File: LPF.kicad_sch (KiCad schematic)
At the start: 1 part

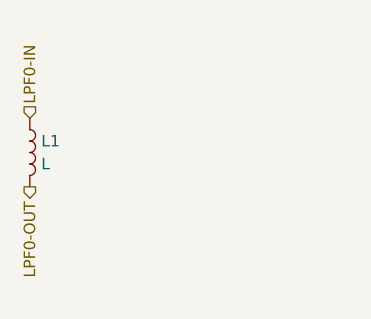
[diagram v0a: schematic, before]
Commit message: placed LPF chains in sub-schematic.  ERC passes
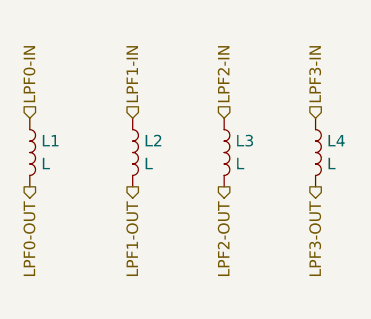
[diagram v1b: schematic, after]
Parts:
- added L2, L3, L4: L, symbol Device:L
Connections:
- new net LPF1-IN: L2.1
- new net LPF1-OUT: L2.2
- new net LPF2-IN: L3.1
- new net LPF2-OUT: L3.2
- new net LPF3-IN: L4.1
- new net LPF3-OUT: L4.2

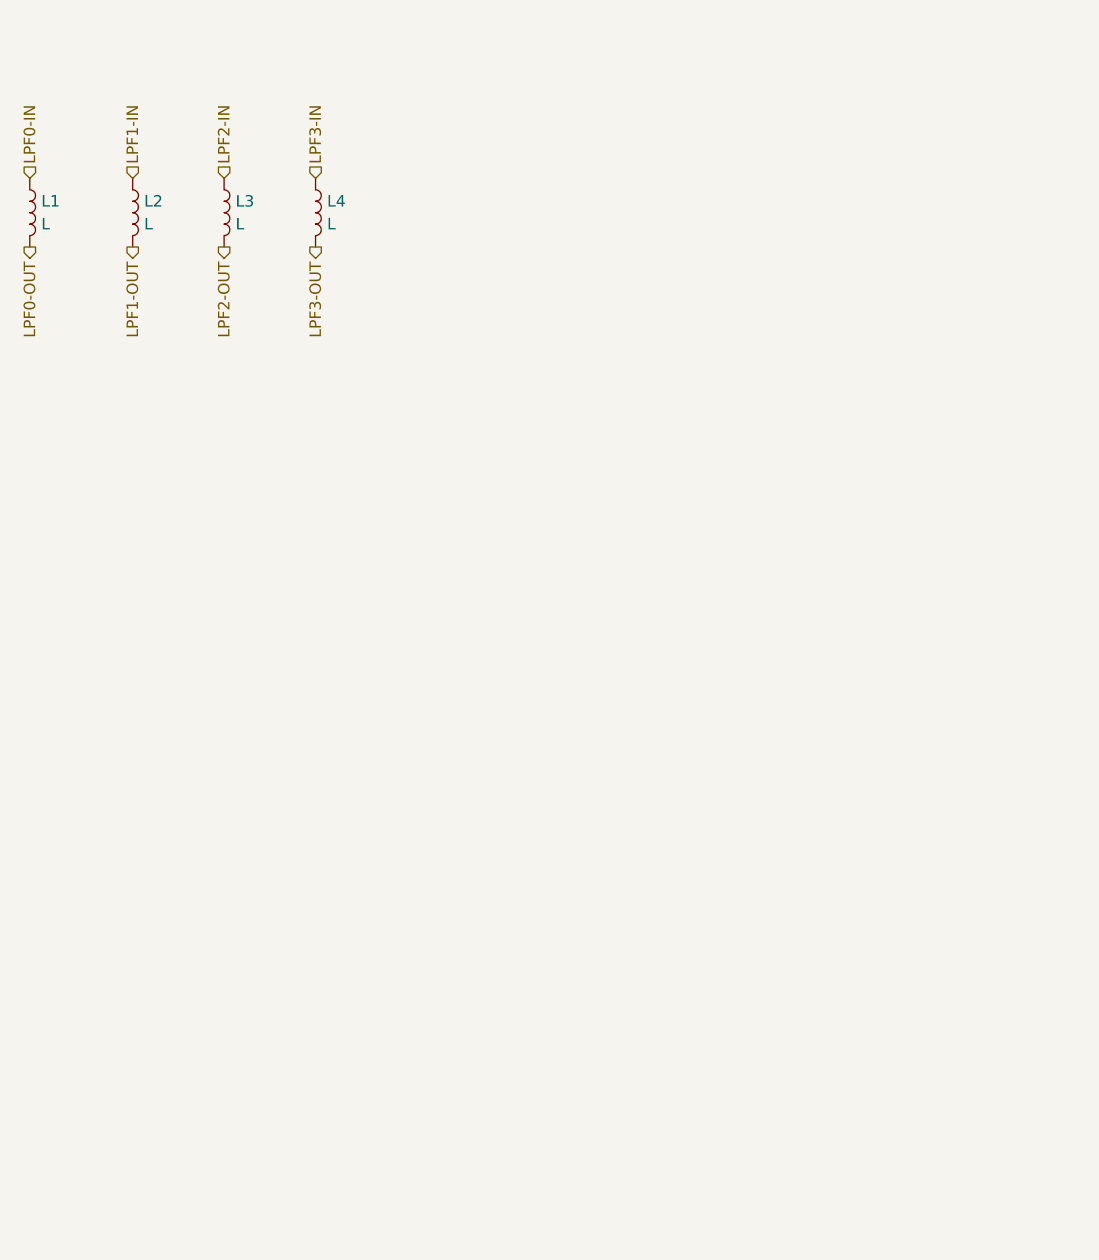
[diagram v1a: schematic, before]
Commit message: fleshed out LPF chains.  ERC passes
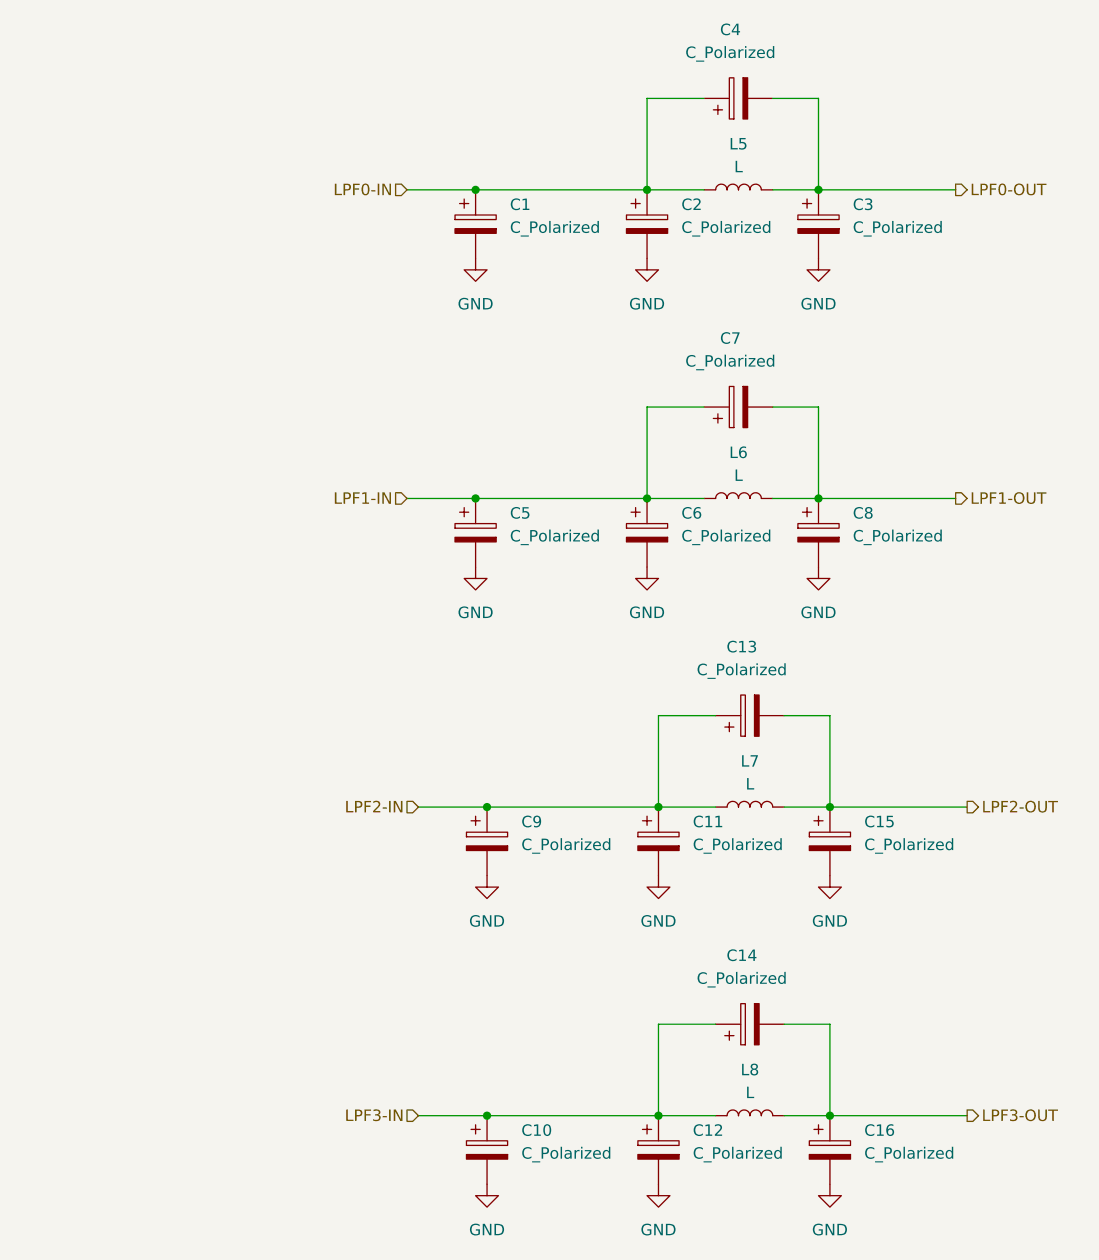
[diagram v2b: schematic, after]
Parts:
- removed L1, L2, L3, L4: L, symbol Device:L
- added C1, C10, C11, C12, C13, C14, C15, C16, C2, C3, C4, C5, C6, C7, C8, C9: C_Polarized, symbol Device:C_Polarized
- added L5, L6, L7, L8: L, symbol Device:L
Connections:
- net LPF0-IN: now also C1.1, C2.1, C4.1, L5.1
- net LPF0-OUT: now also C3.1, C4.2, L5.2
- net LPF1-IN: now also C5.1, C6.1, C7.1, L6.1
- net LPF1-OUT: now also C7.2, C8.1, L6.2
- net LPF2-IN: now also C11.1, C13.1, C9.1, L7.1
- net LPF2-OUT: now also C13.2, C15.1, L7.2
- net LPF3-IN: now also C10.1, C12.1, C14.1, L8.1
- net LPF3-OUT: now also C14.2, C16.1, L8.2
- new net GND: C1.2, C10.2, C11.2, C12.2, C15.2, C16.2, C2.2, C3.2, C5.2, C6.2, C8.2, C9.2

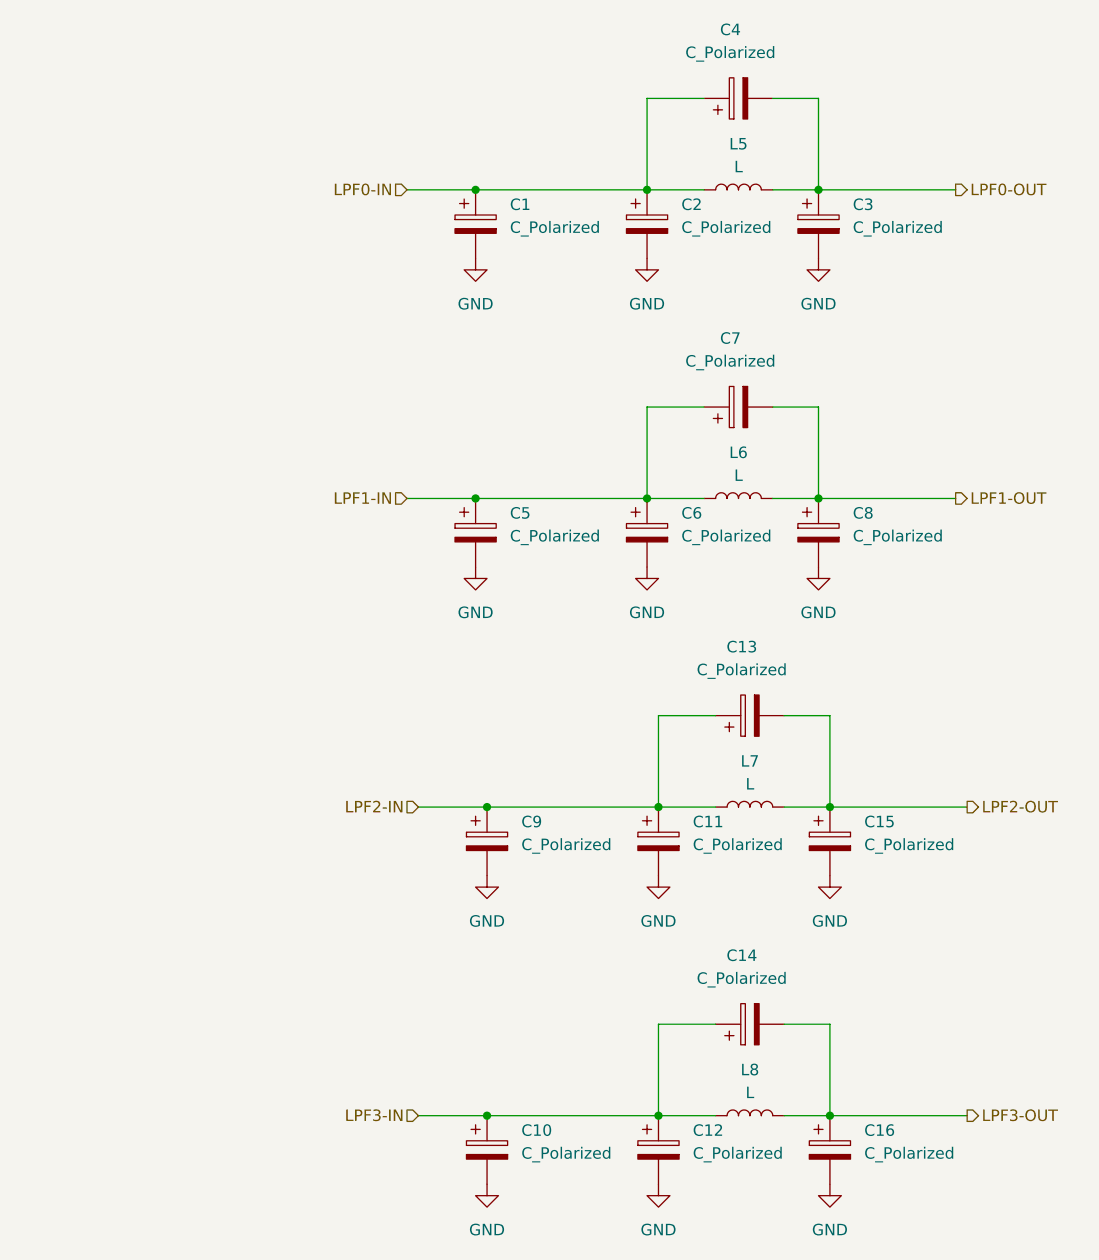
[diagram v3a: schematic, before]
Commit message: LPF chains, all caps now normal; missing inducator added.  ERC passes
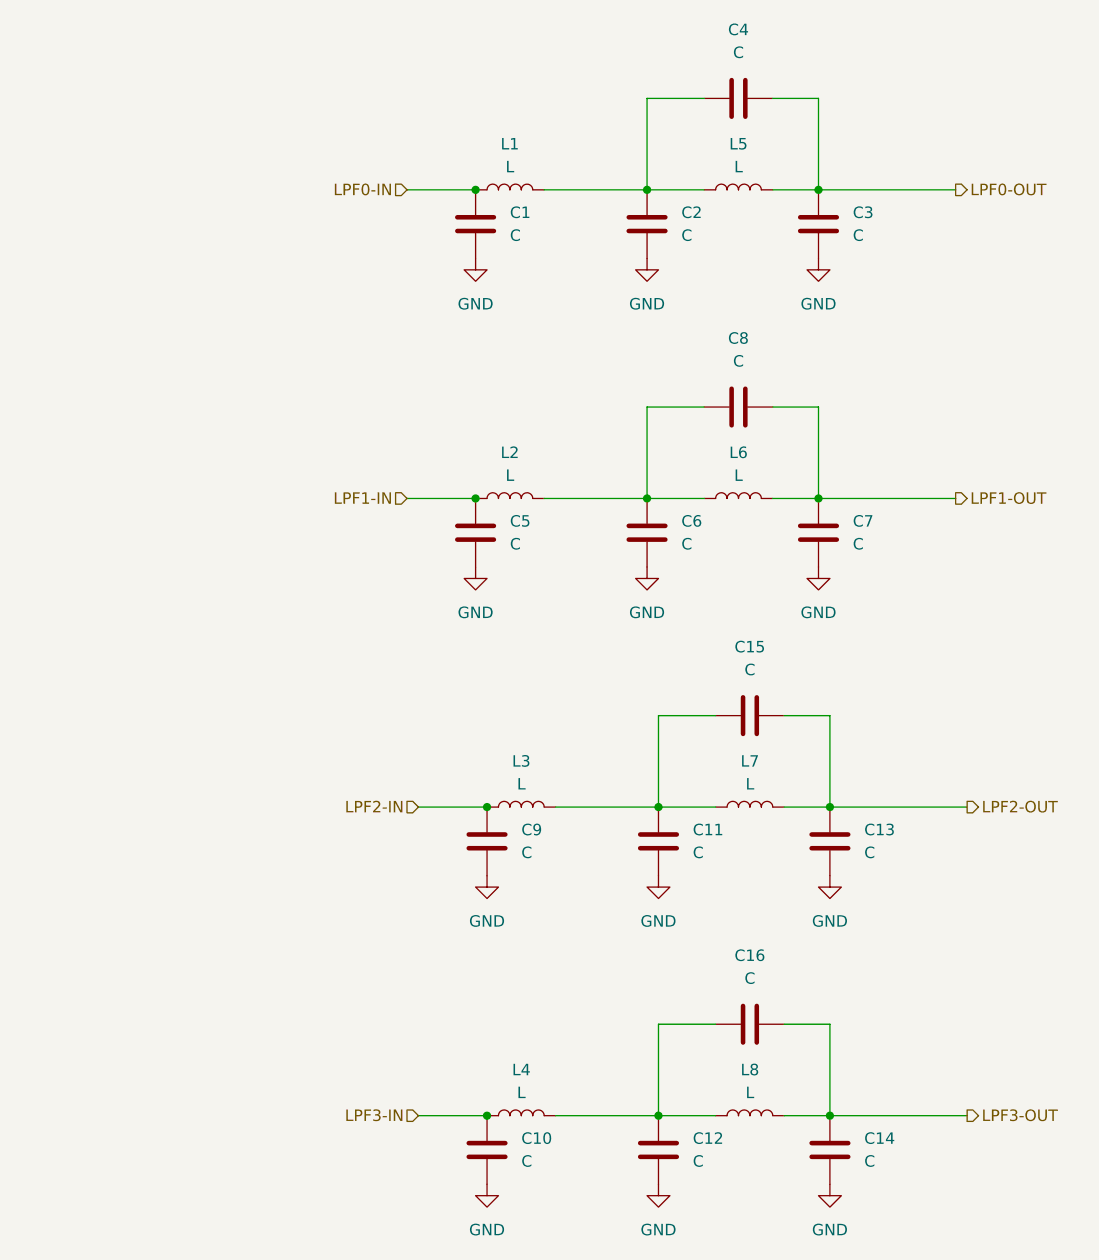
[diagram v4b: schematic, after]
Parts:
- removed C1, C10, C11, C12, C13, C14, C15, C16, C2, C3, C4, C5, C6, C7, C8, C9: C_Polarized, symbol Device:C_Polarized
- added C1, C10, C11, C12, C13, C14, C15, C16, C2, C3, C4, C5, C6, C7, C8, C9: C, symbol Device:C
- added L1, L2, L3, L4: L, symbol Device:L
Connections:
- net GND: now also C1.2, C10.2, C11.2, C12.2, C13.2, C14.2, C2.1, C3.2, C5.2, C6.2, C7.2, C9.2
- net LPF0-IN: now also C1.1, L1.1; no longer L5.1
- net LPF0-OUT: now also C3.1, C4.2
- net LPF1-IN: now also C5.1, L2.1; no longer L6.1
- net LPF1-OUT: now also C7.1, C8.2
- net LPF2-IN: now also C9.1, L3.1; no longer L7.1
- net LPF2-OUT: now also C13.1, C15.2
- net LPF3-IN: now also C10.1, L4.1; no longer L8.1
- net LPF3-OUT: now also C14.1, C16.2
- new net: C2.2, C4.1, L1.2, L5.1
- new net: C6.1, C8.1, L2.2, L6.1
- new net: C12.1, C16.1, L4.2, L8.1
- new net: C11.1, C15.1, L3.2, L7.1

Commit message: all caps on LPF Chain are pF.  rest are uF
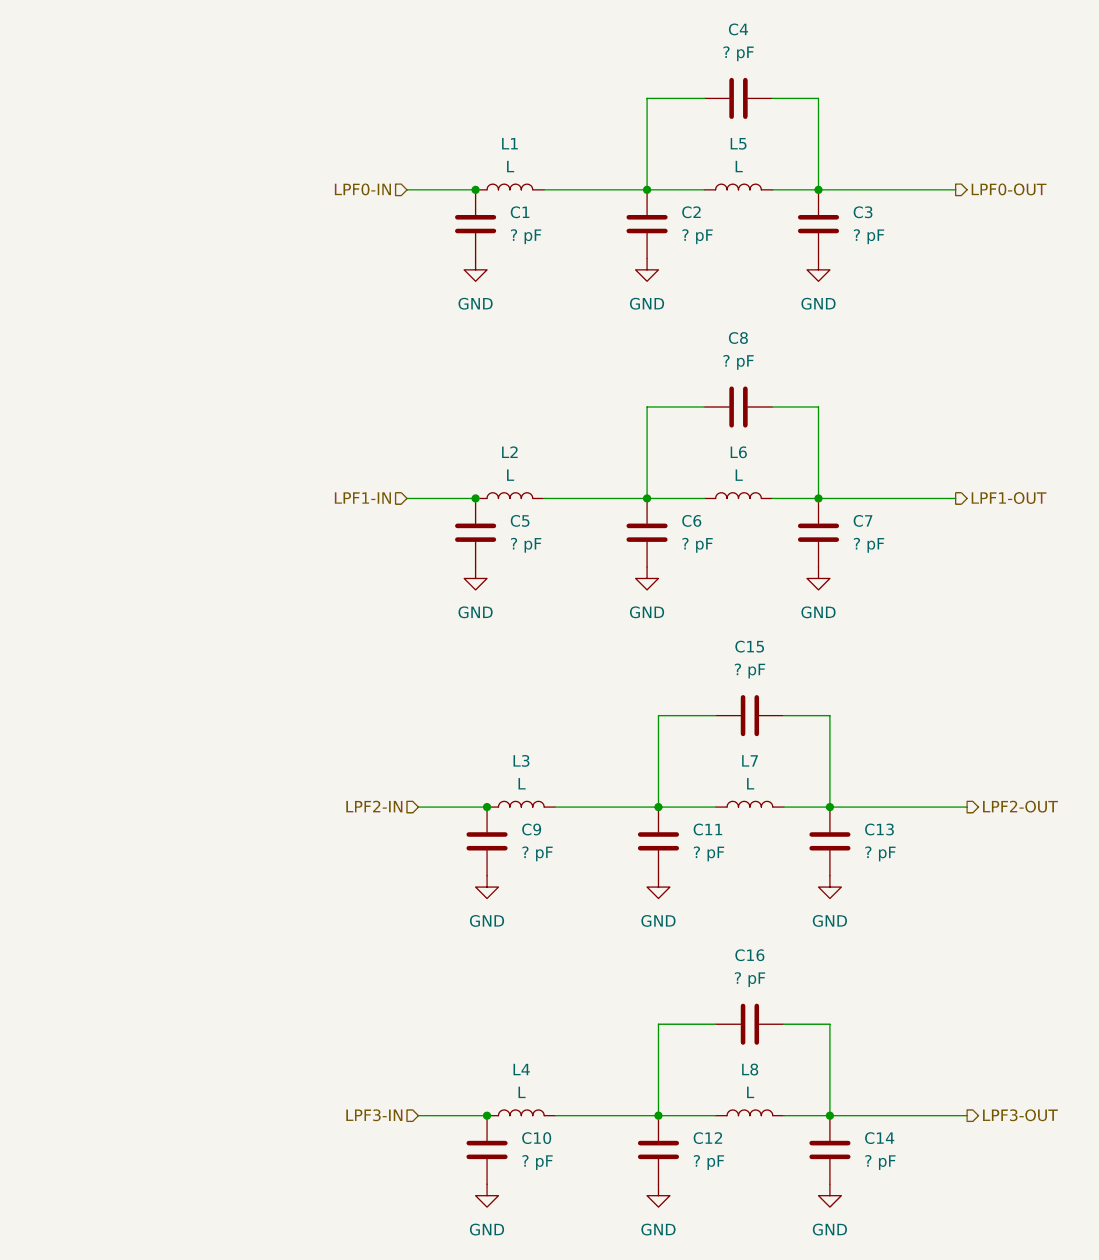
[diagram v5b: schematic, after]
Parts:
- C1, C10, C11, C12, C13, C14, C15, C16, C2, C3, C4, C5, C6, C7, C8, C9: value C -> ? pF
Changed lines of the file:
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@@
 	(title_block
 		(title "QMX Amp")
-		(date "2024-08-09")
-		(rev "v0.1")
+		(date "2024-08-10")
+		(rev "v0.2")
 		(company "WA7GIL")
 	)
@@
 			)
 		)
-		(property "Value" "C"
+		(property "Value" "? pF"
 			(at 104.14 46.9899 0)
 			(effects
@@
 			)
 		)
-		(property "Value" "C"
+		(property "Value" "? pF"
 			(at 129.54 26.67 90)
 			(effects
@@
 			)
 		)
-		(property "Value" "C"
+		(property "Value" "? pF"
 			(at 142.24 46.9899 0)
 			(effects
@@
 			)
 		)
-		(property "Value" "C"
+		(property "Value" "? pF"
 			(at 124.46 149.8599 0)
 			(effects
@@
 			)
 		)
-		(property "Value" "C"
+		(property "Value" "? pF"
 			(at 105.41 149.8599 0)
 			(effects
@@
 			)
 		)
-		(property "Value" "C"
+		(property "Value" "? pF"
 			(at 129.54 60.96 90)
 			(effects
@@
 			)
 		)
-		(property "Value" "C"
+		(property "Value" "? pF"
 			(at 124.46 115.5699 0)
 			(effects
@@
 			)
 		)
-		(property "Value" "C"
+		(property "Value" "? pF"
 			(at 130.81 95.25 90)
 			(effects
@@
 			)
 		)
-		(property "Value" "C"
+		(property "Value" "? pF"
 			(at 123.19 46.9899 0)
 			(effects
@@
 			)
 		)
-		(property "Value" "C"
+		(property "Value" "? pF"
 			(at 105.41 115.5699 0)
 			(effects
@@
 			)
 		)
-		(property "Value" "C"
+		(property "Value" "? pF"
 			(at 143.51 149.8599 0)
 			(effects
@@
 			)
 		)
-		(property "Value" "C"
+		(property "Value" "? pF"
 			(at 104.14 81.2799 0)
 			(effects
@@
 			)
 		)
-		(property "Value" "C"
+		(property "Value" "? pF"
 			(at 142.24 81.2799 0)
 			(effects
@@
 			)
 		)
-		(property "Value" "C"
+		(property "Value" "? pF"
 			(at 130.81 129.54 90)
 			(effects
@@
 			)
 		)
-		(property "Value" "C"
+		(property "Value" "? pF"
 			(at 123.19 81.2799 0)
 			(effects
@@
 			)
 		)
-		(property "Value" "C"
+		(property "Value" "? pF"
 			(at 143.51 115.5699 0)
 			(effects
